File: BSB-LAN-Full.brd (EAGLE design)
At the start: 86.5 x 33 mm, 122 parts, among them IC1 LAN8710A-EZC, IC2 TPS2376D, IC3 TX4138, IC4 SY8089AAAC, IC6 CH340X, Q1 BC847, Q2 BC857, Q3 BC847, Q4 WPM2015-3/TR, Q5 BC847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

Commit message: Correct Component Rotation Values in JLC CPL
Add rotation correction factors to parts which import in the wrong orientation.
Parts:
- UEXT: value DNI -> 2x5 IDC
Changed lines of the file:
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@@
 <attribute name="LCSC_PART" value="C130417" x="-28.46" y="-5.69" size="1.778" layer="28" rot="MR0" display="off"/>
 <attribute name="NAME" x="15.65" y="28.6" size="0.8" layer="26" font="vector" ratio="15" rot="MR270" align="center"/>
+<attribute name="JLC_ROT" value="270" x="13.45" y="28.6" size="1.778" layer="28" rot="MR0" display="off"/>
 </element>
 <element name="Q2" library="BSB-LAN" package="SOT23-BEC" value="BC857" x="35.15" y="28.5" smashed="yes" rot="R270">
 <attribute name="LCSC_PART" value="C426782" x="-4.22" y="13.26" size="1.778" layer="27" rot="R270" display="off"/>
 <attribute name="NAME" x="35.2555" y="30.687" size="0.8" layer="25" font="vector" ratio="15" rot="R180" align="center"/>
-</element>
-<element name="UEXT" library="BSB-LAN" package="ML10" value="DNI" x="55" y="19" smashed="yes" rot="R270">
+<attribute name="JLC_ROT" value="270" x="35.15" y="28.5" size="1.778" layer="27" rot="R270" display="off"/>
+</element>
+<element name="UEXT" library="BSB-LAN" package="ML10" value="2x5 IDC" x="55" y="19" smashed="yes" rot="R270">
 <attribute name="NAME" x="55" y="31.45" size="1.2" layer="25" font="vector" ratio="15" rot="R180" align="center"/>
 <attribute name="VALUE" x="49.92" y="19" size="1.778" layer="27" font="vector" ratio="15" rot="R270" align="center"/>
+<attribute name="LCSC_PART" value="C5665" x="55" y="19" size="1.778" layer="27" rot="R270" display="off"/>
 </element>
 <element name="ACT" library="BSB-LAN" package="CHIP-LED0603" value="red" x="4.85" y="19.95" smashed="yes" rot="R90">
@@
 <attribute name="NAME" x="8.2" y="19.945" size="1.2" layer="25" font="vector" ratio="15" rot="R180" align="center"/>
 <attribute name="VALUE" x="4.85" y="21.855" size="1.27" layer="27" font="vector" ratio="15" rot="R180" align="center"/>
+<attribute name="JLC_ROT" value="270" x="4.85" y="19.95" size="1.778" layer="27" rot="R90" display="off"/>
 </element>
 <element name="R3" library="BSB-LAN" package="R0402" value="220R" x="35" y="28.8" smashed="yes" rot="MR0">
@@
 <attribute name="NAME" x="45.3292875" y="26.6" size="0.8" layer="25" font="vector" ratio="15" align="center"/>
 <attribute name="VALUE" x="43.274871875" y="28.474875" size="0.8" layer="27" font="vector" ratio="15" rot="R135" align="center"/>
+<attribute name="JLC_ROT" value="270" x="40.8" y="26" size="1.778" layer="27" rot="R135" display="off"/>
 </element>
 <element name="POE-ETH" library="BSB-LAN" package="HY931147C-SLOT" value="HY931147C-SLOT" x="5.8" y="9.95" smashed="yes" rot="R90">
@@
 <attribute name="NAME" x="3.85" y="0.8" size="1" layer="25" font="vector" ratio="15" align="center"/>
 <attribute name="VALUE" x="9.3" y="9.95" size="1" layer="27" font="vector" ratio="15" rot="R270" align="center"/>
+<attribute name="JLC_ROT" value="270" x="5.8" y="9.95" size="1.778" layer="27" rot="R90" display="off"/>
 </element>
 <element name="Q3" library="BSB-LAN" package="SOT23" value="BC847" x="50.3" y="21.35" smashed="yes" rot="MR180">
 <attribute name="LCSC_PART" value="C130417" x="50.3" y="21.35" size="1" layer="28" font="vector" ratio="15" rot="MR180" display="off"/>
 <attribute name="NAME" x="50.3055" y="23.463" size="0.8" layer="26" font="vector" ratio="15" rot="MR0" align="center"/>
+<attribute name="JLC_ROT" value="270" x="50.3" y="21.35" size="1.778" layer="28" rot="MR180" display="off"/>
 </element>
 <element name="Q4" library="BSB-LAN" package="SOT23" value="WPM2015-3/TR" x="47.5" y="18.85" smashed="yes">
 <attribute name="LCSC_PART" value="C7472861" x="47.5" y="18.85" size="1" layer="27" font="vector" ratio="15" display="off"/>
 <attribute name="NAME" x="49.0445" y="20.213" size="0.8" layer="25" font="vector" ratio="15" align="center"/>
+<attribute name="JLC_ROT" value="270" x="47.5" y="18.85" size="1.778" layer="27" display="off"/>
 </element>
 <element name="U1" library="BSB-LAN" package="DBV0005A-SOT23" value="ESDS314DBV" x="19.75" y="19.65" smashed="yes" rot="R270">
@@
 <attribute name="VALUE" x="45.8" y="27.645" size="1.016" layer="28" font="vector" ratio="15" rot="MR0" align="center"/>
 <attribute name="LCSC_PART" value="C414564" x="45.8" y="29.55" size="1.778" layer="28" rot="MR0" display="off"/>
+<attribute name="JLC_ROT" value="270" x="45.8" y="29.55" size="1.778" layer="28" rot="MR0" display="off"/>
 </element>
 <element name="RN2" library="BSB-LAN" package="CTS742C083" value="2.2k" x="49.8" y="29.55" smashed="yes" rot="MR0">
@@
 <attribute name="VALUE" x="49.8" y="27.645" size="1.016" layer="28" font="vector" ratio="15" rot="MR0" align="center"/>
 <attribute name="LCSC_PART" value="C414564" x="49.8" y="29.55" size="1.778" layer="28" rot="MR0" display="off"/>
+<attribute name="JLC_ROT" value="270" x="49.8" y="29.55" size="1.778" layer="28" rot="MR0" display="off"/>
 </element>
 <element name="R13" library="BSB-LAN" package="R0402" value="10k" x="49.25" y="16.3" smashed="yes" rot="R180">
@@
 <attribute name="NAME" x="63.45" y="6.525" size="0.8" layer="25" font="vector" ratio="15" align="center"/>
 <attribute name="VALUE" x="63.45" y="12.275" size="1.27" layer="27" font="vector" ratio="15" rot="R180" align="center"/>
+<attribute name="JLC_ROT" value="270" x="63.45" y="9.1" size="1.778" layer="27" rot="R180" display="off"/>
 </element>
 <element name="ESP1" library="BSB-LAN" package="ESP32-WROOM-32E" value="ESP32-WROOM-32E" x="68.8" y="21.8" smashed="yes" rot="R270">
@@
 <attribute name="VALUE" x="84.8" y="21.8" size="0.8" layer="27" font="vector" ratio="15" rot="R270" align="center"/>
 <attribute name="NAME" x="78.6" y="10.9" size="0.8" layer="25" font="vector" ratio="15" align="center"/>
+<attribute name="JLC_ROT" value="270" x="68.8" y="21.8" size="1.778" layer="27" rot="R270" display="off"/>
 </element>
 <element name="USD" library="BSB-LAN" package="MICRO-SD" value="XKTF-001A" x="86.2" y="11.85" smashed="yes" rot="MR90">
@@
 <attribute name="VALUE" x="66.45" y="17.695" size="1.016" layer="28" font="vector" ratio="15" rot="MR0" align="center"/>
 <attribute name="LCSC_PART" value="C414564" x="66.45" y="19.6" size="1.778" layer="28" rot="MR0" display="off"/>
+<attribute name="JLC_ROT" value="270" x="66.45" y="19.6" size="1.778" layer="28" rot="MR0" display="off"/>
 </element>
 <element name="R31" library="BSB-LAN" package="R0402" value="220R" x="76.7" y="27.35" smashed="yes" rot="MR180">
@@
 <attribute name="LCSC_PART" value="C130417" x="82.85" y="11.45" size="1.2" layer="28" font="vector" ratio="15" rot="MR0" display="off"/>
 <attribute name="NAME" x="79.2555" y="8.513" size="0.8" layer="26" font="vector" ratio="15" rot="MR0" align="center"/>
+<attribute name="JLC_ROT" value="270" x="77.85" y="7.05" size="1.778" layer="28" rot="MR0" display="off"/>
 </element>
 <element name="R45" library="BSB-LAN" package="R0402" value="1k" x="80.1" y="6.85" smashed="yes" rot="MR90">
@@
 <attribute name="LCSC_PART" value="C130417" x="82.65" y="5.25" size="1.2" layer="28" font="vector" ratio="15" rot="MR90" display="off"/>
 <attribute name="NAME" x="85.15" y="5.25" size="0.8" layer="26" font="vector" ratio="15" rot="MR180" align="center"/>
+<attribute name="JLC_ROT" value="270" x="82.65" y="5.25" size="1.778" layer="28" rot="MR90" display="off"/>
 </element>
 <element name="R46" library="BSB-LAN" package="R0402" value="1k" x="77.25" y="4.5" smashed="yes" rot="MR0">
@@
 <attribute name="LCSC_PART" value="C7472861" x="66.15" y="-2.15" size="1.2" layer="27" font="vector" ratio="15" rot="R180" display="off"/>
 <attribute name="NAME" x="63.3945" y="2.763" size="0.8" layer="25" font="vector" ratio="15" align="center"/>
+<attribute name="JLC_ROT" value="270" x="60.95" y="2.25" size="1.778" layer="27" rot="R180" display="off"/>
 </element>
 <element name="D6" library="BSB-LAN" package="SMB" value="SS510B" x="59.9" y="5.4" smashed="yes" rot="MR270">
@@
 <attribute name="NAME" x="81.1" y="6.555" size="1.27" layer="25" font="vector" ratio="15" align="center"/>
 <attribute name="VALUE" x="83.305" y="4.45" size="1.27" layer="27" font="vector" ratio="15" rot="R90" align="center"/>
+<attribute name="JLC_ROT" value="270" x="81.4" y="4.45" size="1.778" layer="27" display="off"/>
 </element>
 <element name="C26" library="BSB-LAN" package="C0603L" value="0.1uF" x="72.55" y="9.7" smashed="yes" rot="MR0">

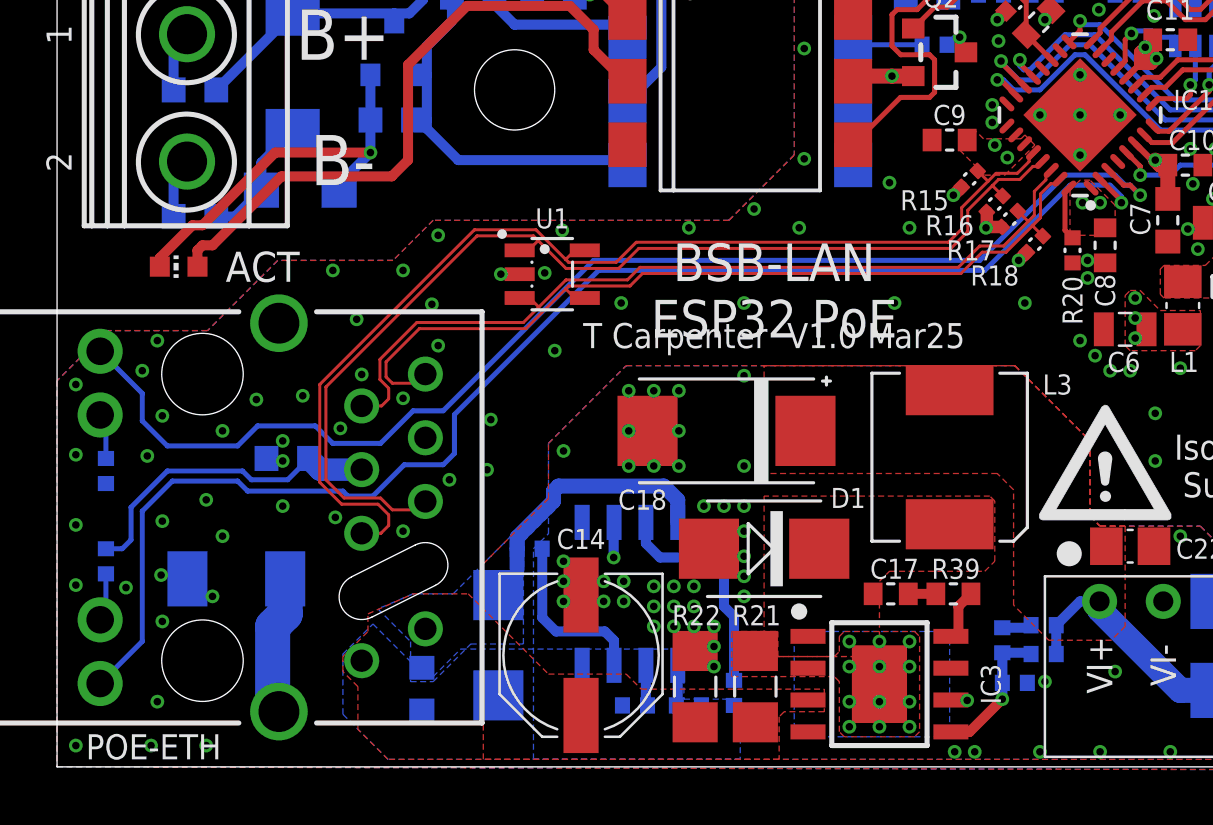
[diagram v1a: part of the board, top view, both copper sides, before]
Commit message: Change Stackup to JLC Default 4L
Use the default stack-up using 7628 to allow the use of Economic assembly. Update trace widths of diff pairs accordingly.
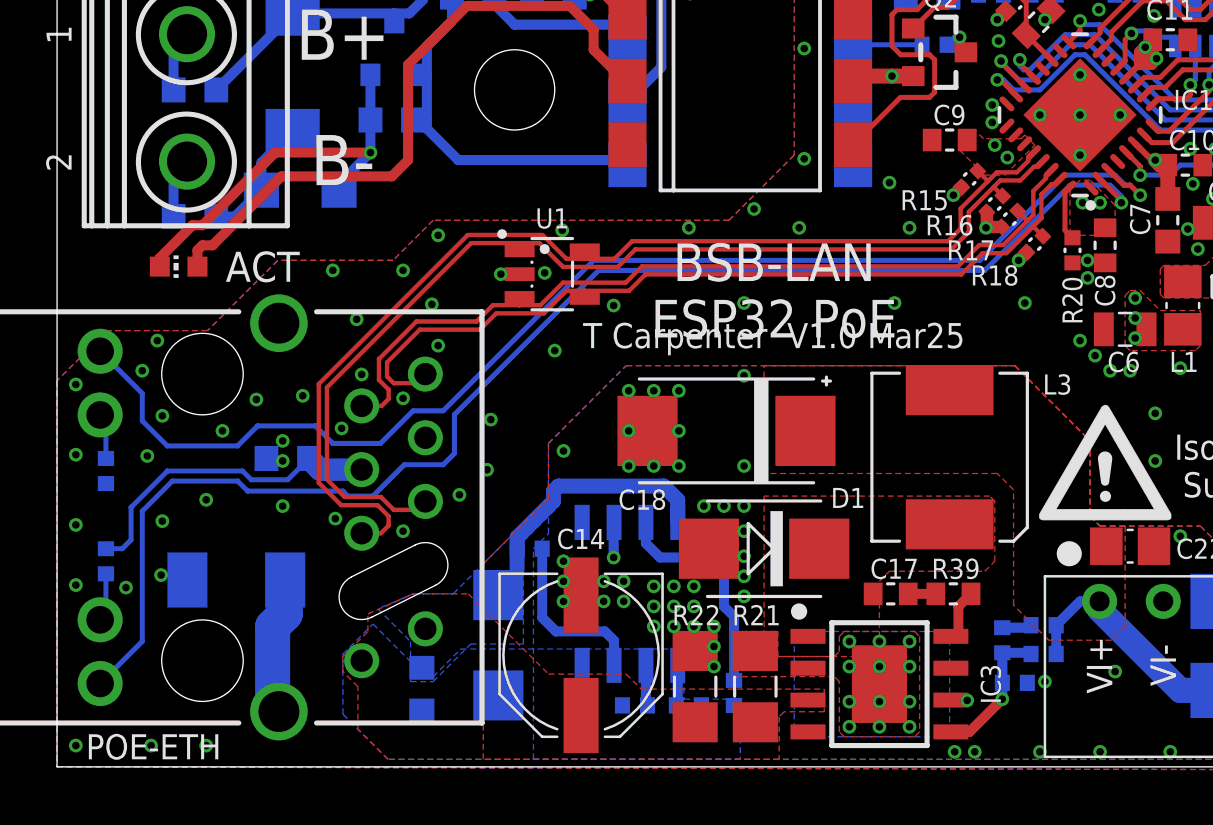
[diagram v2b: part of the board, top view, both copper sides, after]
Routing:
- net ETH-TD_P: track 43.7 -> 42.6 mm
- net ETH-TD_N: track 44.3 -> 43.4 mm
- net ETH-RD_P: track 34.4 -> 33.6 mm
- net ETH-RD_N: track 35.0 -> 34.3 mm

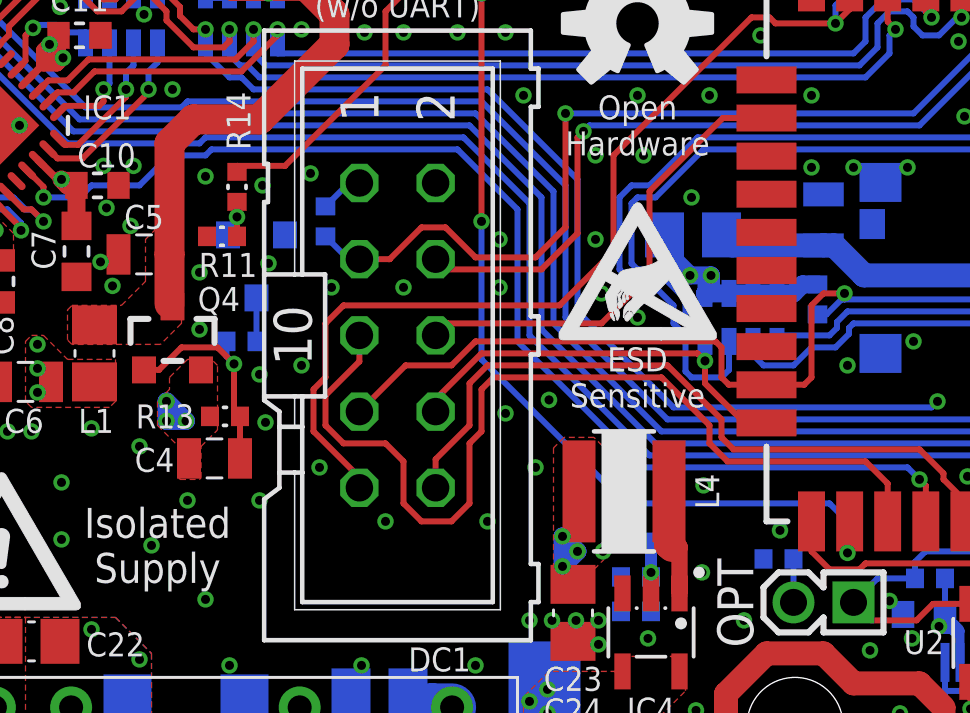
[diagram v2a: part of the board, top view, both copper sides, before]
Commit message: Add Missing Pull-Up Resistors on I2C
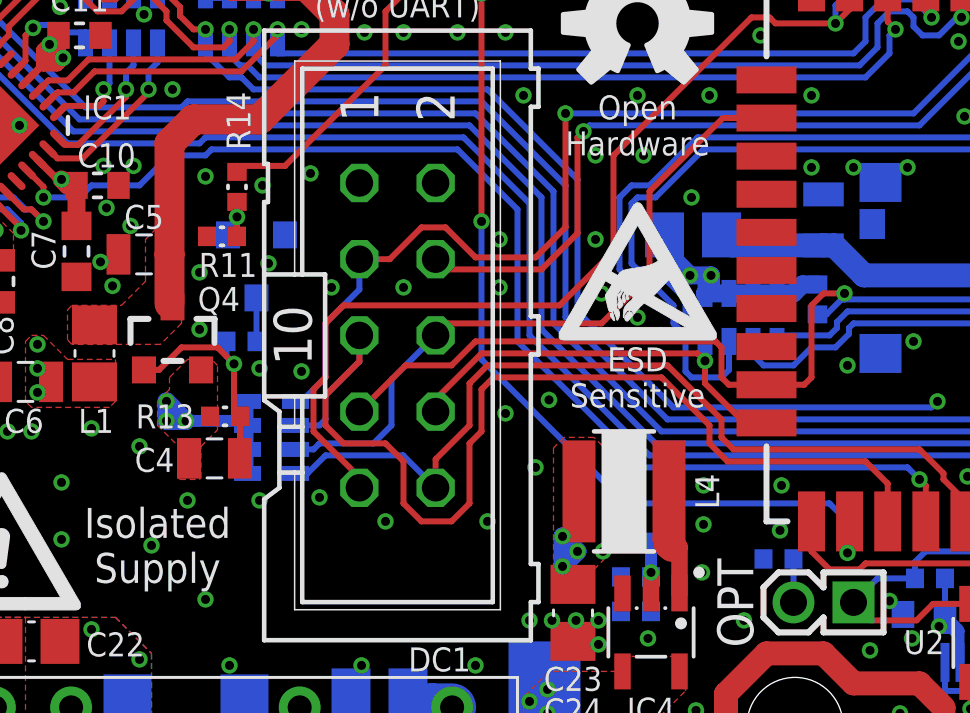
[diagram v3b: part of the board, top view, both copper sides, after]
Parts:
- removed R51: 10k, BSB-LAN:R0402
- added RN4: 2.2k, BSB-LAN:CTS742C083
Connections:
- net +3.3V: now also RN4.5, RN4.6, RN4.7, RN4.8; no longer R51.1
- net ESP-SCL: now also RN4.2
- net ESP-SDA: now also RN4.3
- net ESP-SSEL: now also RN4.4
- net UEXT-TX: now also RN4.1; no longer R51.2
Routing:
- net ESP-SDA: track 15.7 -> 22.8 mm
- net ESP-SSEL: track 23.7 -> 29.1 mm
- net ESP-SCL: track 31.4 -> 35.8 mm
- net UEXT-TX: track 30.6 -> 34.9 mm
- net +3.3V: track 52.8 -> 54.4 mm

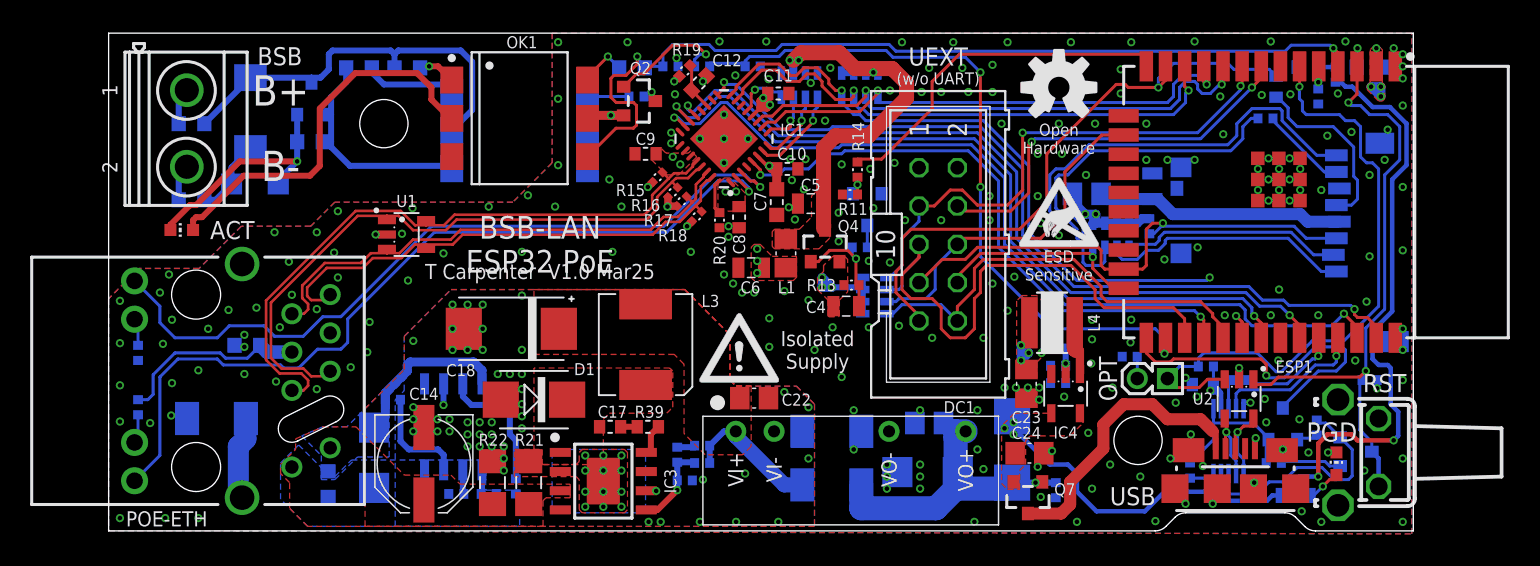
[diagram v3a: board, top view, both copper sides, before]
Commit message: Correct Pinout of DC-DC Converter
Not sure quite how I messed up the pin assignments that badly!
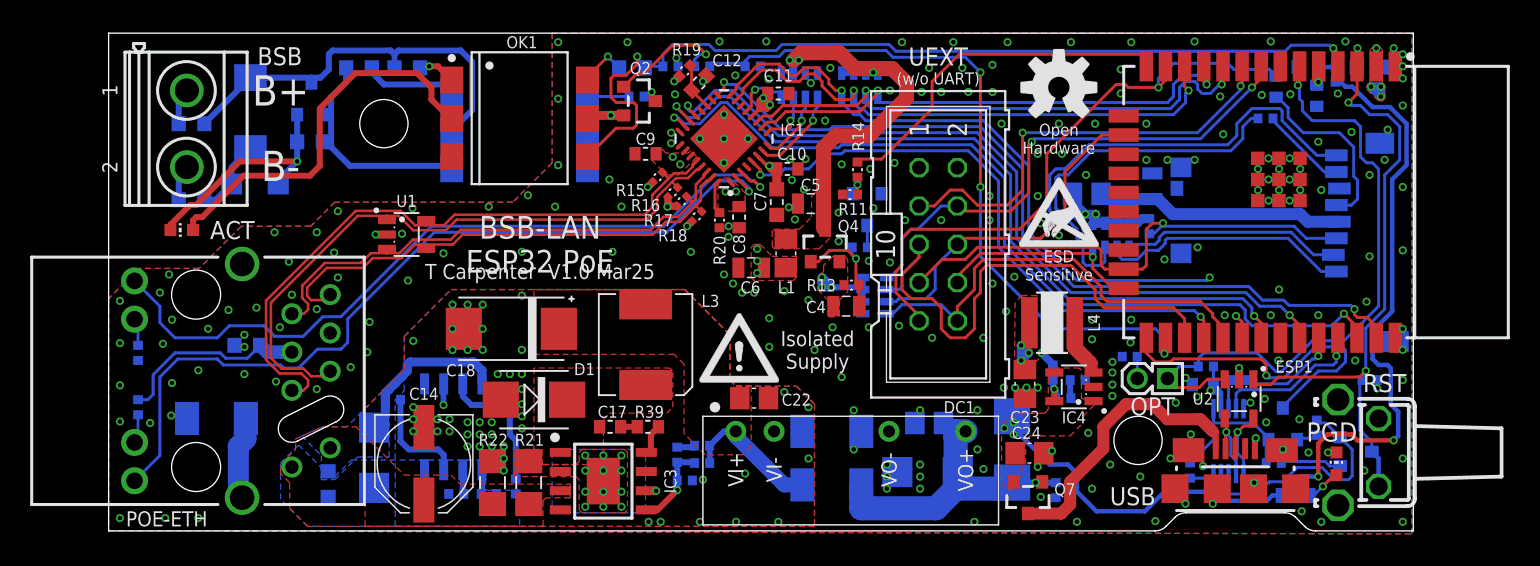
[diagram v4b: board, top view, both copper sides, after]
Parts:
- R43: value 12.1k 1% -> 180k 1%
- R44: value 28.7k 1% -> 330k; device BSB-LAN:R0402 -> BSB-LAN:R0603L
- moved R41 2.18 mm to (63.3, 8.80), turned to 0 degrees
- moved R40 1.64 mm to (62.6, 10.5), turned to 90 degrees
- moved R42 1.32 mm to (64.2, 10.0)
- moved IC4 0.71 mm to (64.0, 9.55), turned to 90 degrees
- moved R44 0.11 mm to (80.1, 28.9)
- moved C23 0.10 mm to (60.8, 9.75)
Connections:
- net +5.0V: now also IC4.1; no longer IC4.5
- net 3V3-FB: now also IC4.5; no longer IC4.2
- net 3V3-LX: now also IC4.3; no longer IC4.1
- net GND: now also IC4.2; no longer IC4.3
- net UEXT-RX: now also RN4.1
- net UEXT-TX: no longer RN4.1
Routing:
- net UEXT-RX: track 26.6 -> 34.3 mm
- net UEXT-TX: track 34.9 -> 29.2 mm
- net PWR-SNS: track 4.66 -> 3.51 mm
